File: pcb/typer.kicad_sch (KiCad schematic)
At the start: 48 parts, among them J2 3.5mm, SW0:10 SW0:3, SW0:11 SW0:2, SW0:12 SW0:1, SW0:7 SW0:6, SW0:8 SW0:5, SW0:9 SW0:4, SW1:10 SW1:3, SW1:11 SW1:2, SW1:12 SW1:1, SW1:13 SW1:0, SW1:9 SW1:4, SW2:10 SW2:3, SW2:11 SW2:2, SW2:12 SW2:1, SW2:13 SW2:0, SW2:7 SW2:6, SW2:8 SW2:5, SW2:9 SW2:4, SW3:10 SW3:3, SW3:11 SW3:2, SW3:12 SW3:1, SW3:13 SW3:0, SW3:8 SW3:5, SW3:9 SW3:4, SW4:10 SW4:3, SW4:11 SW4:2, SW4:12 SW4:1, SW4:13 SW4:0, SW4:7 SW4:6, SW4:8 SW4:5, SW4:9 SW4:4, SW5:10 SW5:3, SW5:11 SW5:2, SW5:12 SW5:1, SW5:13 SW5:0, SW5:7 SW5:6, SW5:8 SW5:5, SW5:9 SW5:4

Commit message: new project updates
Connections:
- net ROW0 is gone; now on an unnamed net: SW0:10.1, SW0:11.1, SW0:12.1, SW0:7.1, SW0:8.1, SW0:9.1, SX0:10.1, SX0:11.1
- net ROW1 is gone; now on an unnamed net: SW1:10.1, SW1:11.1, SW1:12.1, SW1:13.1, SW1:9.1, SX1:7.1, SX1:8.1
- net at D1:8.1 (A), SX1:8.2: now also D1:7.1 (A), D1:7.2 (K), D1:8.2 (K), SW0:10.4 (K), SW0:11.4 (K), SW0:7.4 (K), SW0:8.4 (K), SW1:10.4 (K), SW1:11.4 (K), SW2:10.4 (K), SW2:11.4 (K), SW2:7.4 (K), SW2:8.4 (K), SW3:10.4 (K), SW3:11.4 (K), SW3:8.4 (K), SX1:7.2
- net COL0: no longer names the net of SW1:13.4 (K), SW2:13.4 (K), SW3:13.4 (K)
- net COL0: no longer SW4:13.4 (K), SW5:13.4 (K)
- net COL1: no longer names the net of SW0:12.4 (K), SW1:12.4 (K), SW2:12.4 (K), SW3:12.4 (K)
- net COL1: no longer SW4:12.4 (K), SW5:12.4 (K)
- removed net COL10: SW0:10.4 (K), SW1:10.4 (K), SW2:10.4 (K), SW3:10.4 (K), SW4:10.4 (K), SW5:10.4 (K)
- removed net COL11: SW0:11.4 (K), SW1:11.4 (K), SW2:11.4 (K), SW3:11.4 (K), SW4:11.4 (K), SW5:11.4 (K)
- net COL4: no longer names the net of SW0:9.4 (K), SW1:9.4 (K), SW2:9.4 (K), SW3:9.4 (K)
- net COL4: no longer SW4:9.4 (K), SW5:9.4 (K)
- removed net COL5: D1:8.2 (K), SW0:8.4 (K), SW2:8.4 (K), SW3:8.4 (K), SW4:8.4 (K), SW5:8.4 (K)
- removed net COL6: D1:7.2 (K), SW0:7.4 (K), SW2:7.4 (K), SW4:7.4 (K), SW5:7.4 (K)
- net ROW2: no longer names the net of SW2:10.1, SW2:11.1, SW2:12.1, SW2:13.1, SW2:7.1, SW2:8.1, SW2:9.1
- removed net ROW3: SW3:10.1, SW3:11.1, SW3:12.1, SW3:13.1, SW3:8.1, SW3:9.1
- removed net ROW4: SW4:10.1, SW4:11.1, SW4:12.1, SW4:13.1, SW4:7.1, SW4:8.1, SW4:9.1
- removed net ROW5: SW5:10.1, SW5:11.1, SW5:12.1, SW5:13.1, SW5:7.1, SW5:8.1, SW5:9.1
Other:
- note added: "Mounting Holes"
- moved on the sheet: D1:7, D1:8, H99, J2, S1, S2, SW0:10, SW0:11, SW0:12, SW0:7, SW0:8, SW0:9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

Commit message: placement update
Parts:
- removed D1:7, D1:8: D, symbol Library:DIODE
- H99: footprint (none) -> Library:ErgoDOXmech
- J2: footprint (none) -> Library:4pin35mmAudio
- S1, S2: footprint (none) -> Library:STAB_PCB940
- SW0:0: renamed from SW5:13; value SW5:0 -> SW0:0; footprint (none) -> Library:MX_FLIP_XX
- SW0:1: renamed from SW4:13; value SW4:0 -> SW0:1; footprint (none) -> Library:MX_FLIP_XX
- SW0:2: renamed from SW3:13; value SW3:0 -> SW0:2; footprint (none) -> Library:MX_FLIP_XX
- SW0:3: renamed from SW2:13; value SW2:0 -> SW0:3; footprint (none) -> Library:MX_FLIP_XX
- SW0:4: renamed from SW1:13; value SW1:0 -> SW0:4; footprint (none) -> Library:MX_FLIP_DIODE
- SW1:0: renamed from SW5:12; value SW5:1 -> SW1:0; footprint (none) -> Library:MX_FLIP_DIODE
- SW1:1: renamed from SW4:12; value SW4:1 -> SW1:1; footprint (none) -> Library:MX_FLIP_DIODE
- SW1:2: renamed from SW3:12; value SW3:1 -> SW1:2; footprint (none) -> Library:MX_FLIP_DIODE
- SW1:3: renamed from SW2:12; value SW2:1 -> SW1:3; footprint (none) -> Library:MX_FLIP_DIODE
- SW1:4: renamed from SW1:12; value SW1:1 -> SW1:4; footprint (none) -> Library:MX_FLIP_DIODE
- SW2:0: renamed from SW5:11; value SW5:2 -> SW2:0; footprint (none) -> Library:MX_FLIP_DIODE
- SW2:1: renamed from SW4:11; value SW4:2 -> SW2:1; footprint (none) -> Library:MX_FLIP_DIODE
- SW2:2: renamed from SW3:11; value SW3:2 -> SW2:2; footprint (none) -> Library:MX_FLIP_DIODE
- SW2:3: renamed from SW2:11; value SW2:2 -> SW2:3; footprint (none) -> Library:MX_FLIP_DIODE
- SW2:4: renamed from SW1:11; value SW1:2 -> SW2:4; footprint (none) -> Library:MX_FLIP_DIODE
- SW3:0: renamed from SW5:10; value SW5:3 -> SW3:0; footprint (none) -> Library:MX_FLIP_DIODE
- SW3:1: renamed from SW4:10; value SW4:3 -> SW3:1; footprint (none) -> Library:MX_FLIP_DIODE
- SW3:2: renamed from SW3:10; value SW3:3 -> SW3:2; footprint (none) -> Library:MX_FLIP_DIODE
- SW3:3: renamed from SW2:10; value SW2:3 -> SW3:3; footprint (none) -> Library:MX_FLIP_DIODE
- SW3:4: renamed from SW1:10; value SW1:3 -> SW3:4; footprint (none) -> Library:MX_FLIP_DIODE
- SW4:0: renamed from SW5:9; value SW5:4 -> SW4:0; footprint (none) -> Library:MX_FLIP_DIODE
- SW4:1: renamed from SW4:9; value SW4:4 -> SW4:1; footprint (none) -> Library:MX_FLIP_DIODE
- SW4:2: renamed from SW3:9; value SW3:4 -> SW4:2; footprint (none) -> Library:MX_FLIP_DIODE
- SW4:3: renamed from SW2:9; value SW2:4 -> SW4:3; footprint (none) -> Library:MX_FLIP_DIODE
- SW4:4: renamed from SW1:9; value SW1:4 -> SW4:4; footprint (none) -> Library:MX_FLIP_DIODE
- SW5:0: renamed from SW5:8; value SW5:5 -> SW5:0; footprint (none) -> Library:MX_FLIP_DIODE
- SW5:1: renamed from SW4:8; value SW4:5 -> SW5:1; footprint (none) -> Library:MX_FLIP_DIODE
- SW5:2: renamed from SW3:8; value SW3:5 -> SW5:2; footprint (none) -> Library:MX_FLIP_DIODE
- SW5:3: renamed from SW2:8; value SW2:5 -> SW5:3; footprint (none) -> Library:MX_FLIP_DIODE
- SW5:4: renamed from SW0:11; value SW0:2 -> SW5:4; footprint (none) -> Library:MX_FLIP_DIODE
- SW6:0: renamed from SW5:7; value SW5:6 -> SW6:0; footprint (none) -> Library:MX_FLIP_DIODE
- SW6:1: renamed from SW4:7; value SW4:6 -> SW6:1; footprint (none) -> Library:MX_FLIP_DIODE
- SW6:2: renamed from SW2:7; value SW2:6 -> SW6:2; footprint (none) -> Library:MX_FLIP_DIODE
- SW6:3: renamed from SW0:12; value SW0:1 -> SW6:3; footprint (none) -> Library:MX_FLIP_DIODE
- SW6:4: renamed from SW0:10; value SW0:3 -> SW6:4; footprint (none) -> Library:MX_FLIP_DIODE
- SW7:2: renamed from SW0:7; value SW0:6 -> SW7:2; footprint (none) -> Library:MX_FLIP_DIODE
- SW7:3: renamed from SW0:8; value SW0:5 -> SW7:3; footprint (none) -> Library:MX_FLIP_DIODE
- SW7:4: renamed from SW0:9; value SW0:4 -> SW7:4; footprint (none) -> Library:MX_FLIP_DIODE
- SX5:4: renamed from SX1:7; value SX1:6 -> SX5:4; footprint (none) -> Library:MX_FLIP
- SX6:4: renamed from SX1:8; value SX1:5 -> SX6:4; footprint (none) -> Library:MX_FLIP
- SY5:4: renamed from SX0:11; value SX0:2 -> SY5:4; footprint (none) -> Library:MX_FLIP
- SY6:4: renamed from SX0:10; value SX0:3 -> SY6:4; footprint (none) -> Library:MX_FLIP
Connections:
- net at SW6:4.2, SW6:4.3 (A), SY6:4.2: now also SX6:4.2
- net COLUMN6: now reaches SW6:1.1
- net COLUMN6: now also SW6:0.1, SW6:2.1, SW6:3.1, SW6:4.1, SX6:4.1, SY6:4.1
- net ROW1: now reaches SW6:1.4 (K)
- net ROW1: now also SW0:1.4 (K), SW1:1.4 (K), SW2:1.4 (K), SW3:1.4 (K), SW4:1.4 (K), SW5:1.4 (K)
- net COLUMN5: now reaches SW5:1.1
- net COLUMN5: now also SW5:0.1, SW5:2.1, SW5:3.1, SW5:4.1, SX5:4.1, SY5:4.1
- net COLUMN1: now reaches SW1:1.1
- net COLUMN1: now also SW1:0.1, SW1:2.1, SW1:3.1, SW1:4.1
- net COLUMN2: now reaches SW2:1.1
- net COLUMN2: now also SW2:0.1, SW2:2.1, SW2:3.1, SW2:4.1
- net COLUMN3: now reaches SW3:1.1
- net COLUMN3: now also SW3:0.1, SW3:2.1, SW3:3.1, SW3:4.1
- net COLUMN4: now reaches SW4:1.1
- net COLUMN4: now also SW4:0.1, SW4:2.1, SW4:3.1, SW4:4.1
- net COLUMN0: now reaches SW0:1.1
- net COLUMN0: now also SW0:0.1, SW0:2.1, SW0:3.1, SW0:4.1
- net ROW4: now reaches SW4:4.4 (K), SW7:4.4 (K)
- net ROW4: now also SW0:4.4 (K), SW1:4.4 (K), SW2:4.4 (K), SW3:4.4 (K), SW5:4.4 (K), SW6:4.4 (K); no longer SW4:2.4 (K), SW4:3.4 (K)
- net at SW5:4.2, SW5:4.3 (A), SY5:4.2: now also SX5:4.2
- net ROW0: now reaches SW0:0.4 (K)
- net ROW0: now also SW1:0.4 (K), SW2:0.4 (K), SW3:0.4 (K), SW4:0.4 (K), SW5:0.4 (K), SW6:0.4 (K)
- new net COLUMN7: SW7:2.1, SW7:3.1, SW7:4.1
- new net ROW2: SW0:2.4 (K), SW1:2.4 (K), SW2:2.4 (K), SW3:2.4 (K), SW4:2.4 (K), SW5:2.4 (K), SW6:2.4 (K), SW7:2.4 (K)
- new net ROW3: SW7:3.4 (K)
- now unconnected: SW0:3.4 (K), SW1:3.4 (K), SW2:3.4 (K), SW3:3.4 (K), SW5:3.4 (K), SW6:3.4 (K)
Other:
- moved on the sheet: SW5:4, SW6:2, SW6:3, SW6:4, SW7:2, SW7:3, SW7:4, SX5:4, SX6:4, SY5:4, SY6:4

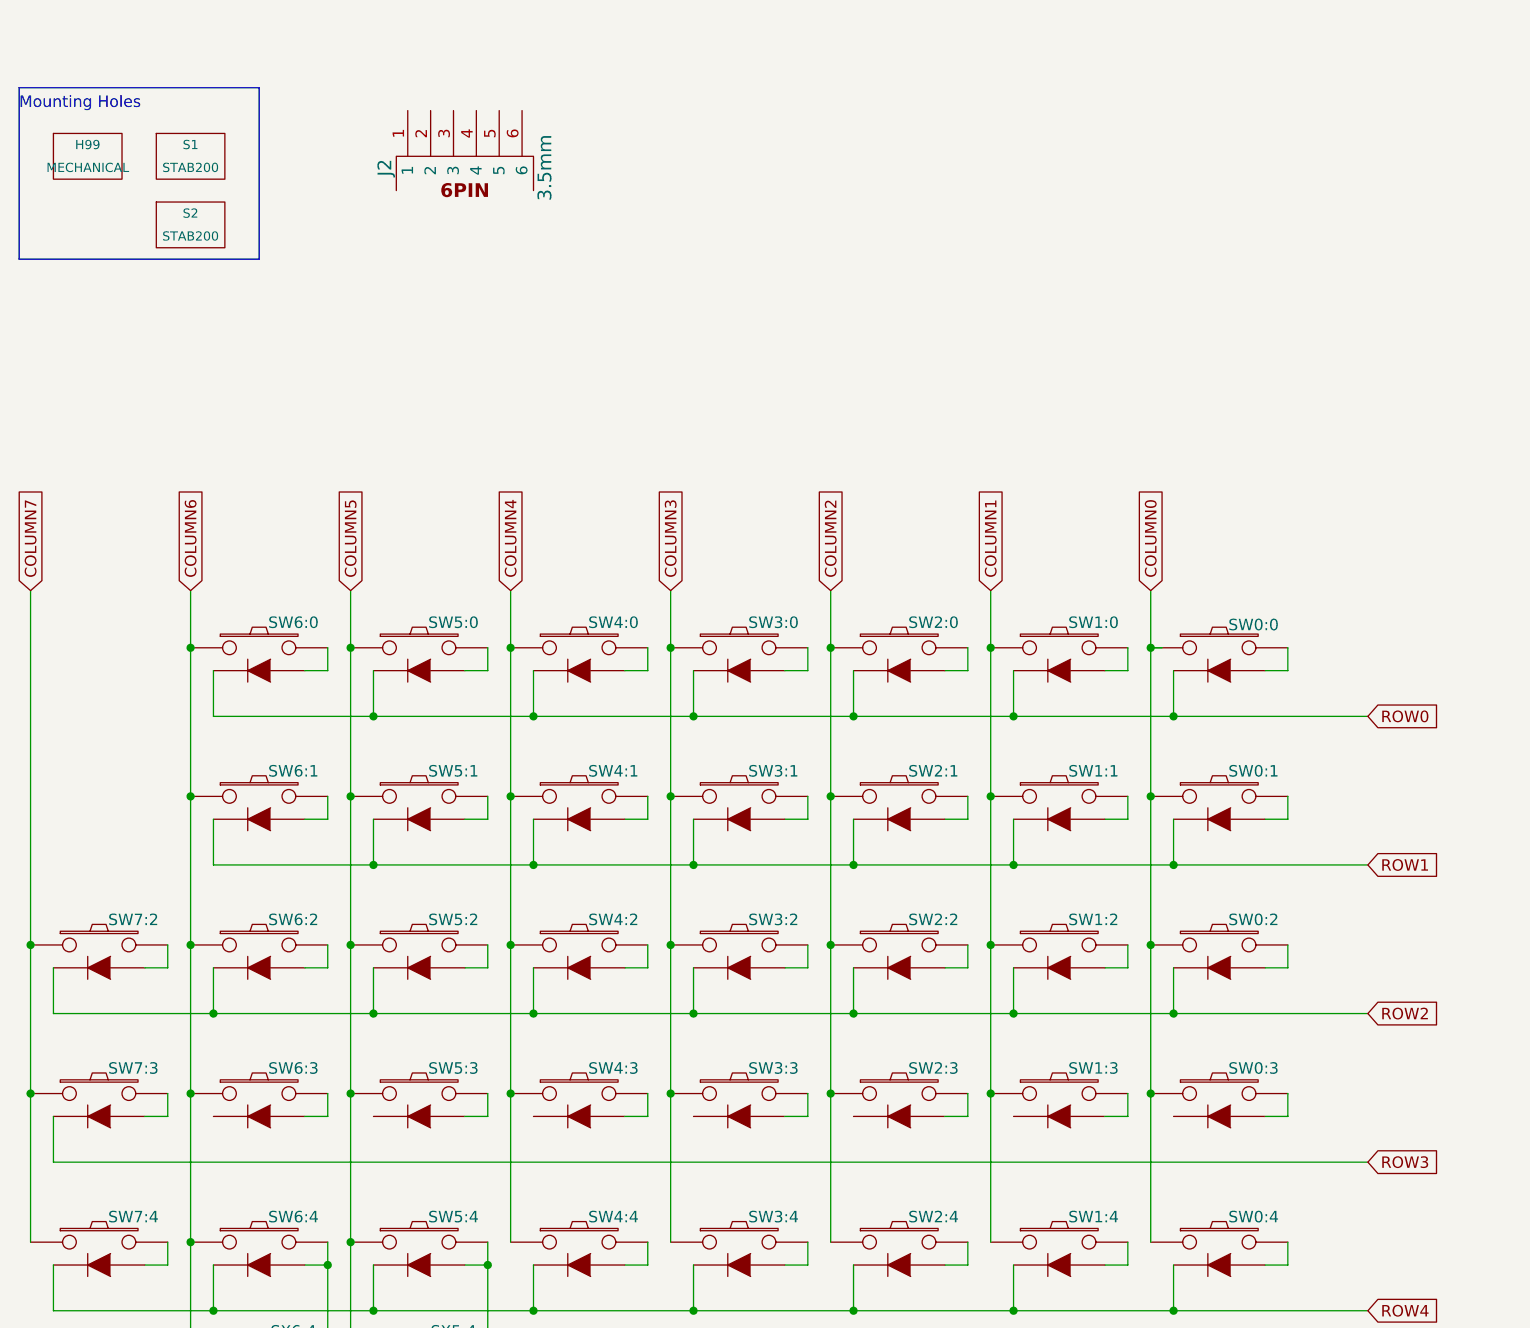
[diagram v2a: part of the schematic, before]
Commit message: row track layout added
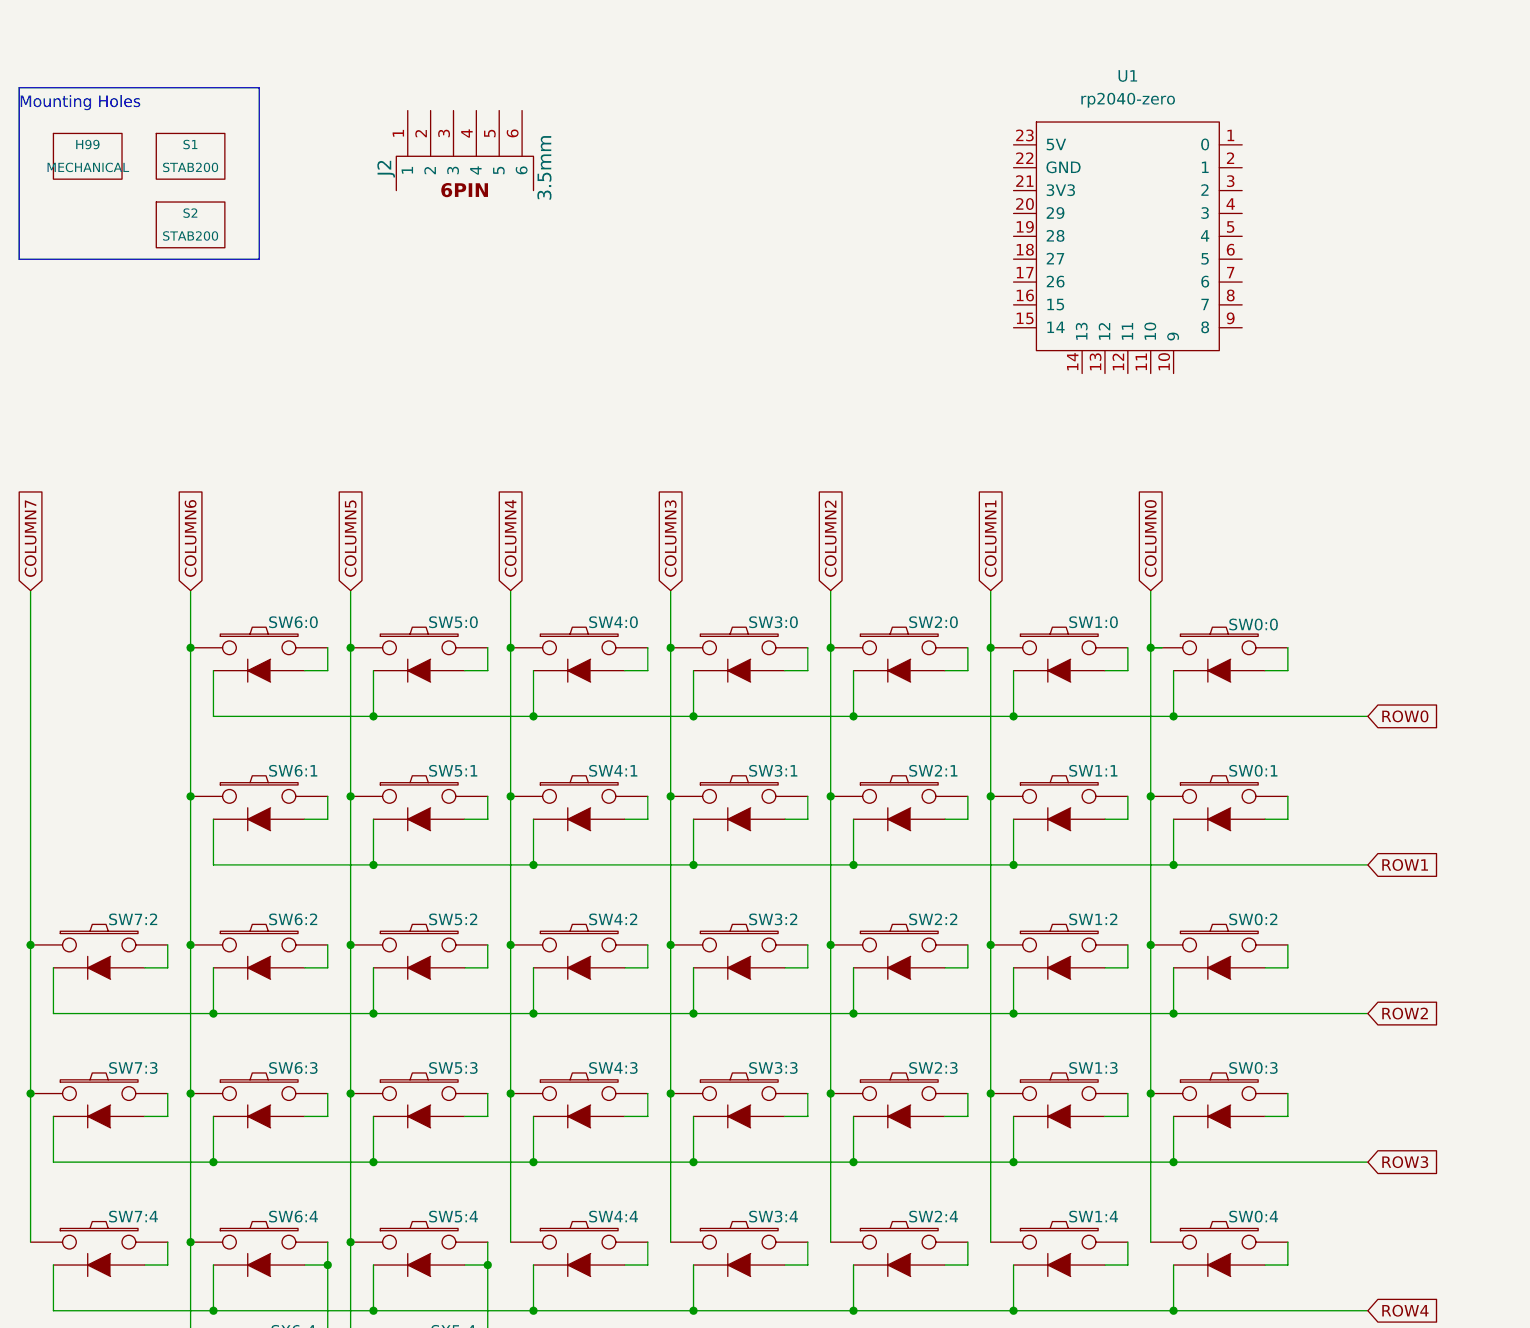
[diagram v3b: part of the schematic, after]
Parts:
- added U1: rp2040-zero, mcu:rp2040-zero-tht, symbol mcu:rp2040-zero
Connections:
- net ROW3: now also SW0:3.4 (K), SW1:3.4 (K), SW2:3.4 (K), SW3:3.4 (K), SW4:3.4 (K), SW5:3.4 (K), SW6:3.4 (K)
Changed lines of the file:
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@@
     (date "29 sep 2012")
   )
+  (junction (at 59.69 143.51) (diameter 0) (color 0 0 0 0)
+  )
   (junction (at 110.49 102.87) (diameter 0) (color 0 0 0 0)
   )
@@
   (junction (at 148.59 127) (diameter 0) (color 0 0 0 0)
   )
+  (junction (at 130.81 143.51) (diameter 0) (color 0 0 0 0)
+  )
+  (junction (at 41.91 143.51) (diameter 0) (color 0 0 0 0)
+  )
   (junction (at 74.93 135.89) (diameter 0) (color 0 0 0 0)
   )
@@
   (junction (at 130.81 93.98) (diameter 0) (color 0 0 0 0)
   )
+  (junction (at 77.47 143.51) (diameter 0) (color 0 0 0 0)
+  )
   (junction (at 146.05 102.87) (diameter 0) (color 0 0 0 0)
   )
@@
   (junction (at 95.25 110.49) (diameter 0) (color 0 0 0 0)
   )
+  (junction (at 113.03 143.51) (diameter 0) (color 0 0 0 0)
+  )
   (junction (at 92.71 86.36) (diameter 0) (color 0 0 0 0)
   )
@@
   (junction (at 57.15 165.1) (diameter 0) (color 0 0 0 0)
   )
+  (junction (at 148.59 143.51) (diameter 0) (color 0 0 0 0)
+  )
   (junction (at 39.37 135.89) (diameter 0) (color 0 0 0 0)
   )
+  (junction (at 95.25 143.51) (diameter 0) (color 0 0 0 0)
+  )
   (junction (at 148.59 160.02) (diameter 0) (color 0 0 0 0)
   )
@@
     (stroke (width 0) (type default))
   )
+  (wire (pts (xy 148.59 138.43) (xy 148.59 143.51))
+    (stroke (width 0) (type default))
+  )
   (wire (pts (xy 52.07 138.43) (xy 54.61 138.43))
     (stroke (width 0) (type default))
@@
     (stroke (width 0) (type default))
   )
+  (wire (pts (xy 41.91 143.51) (xy 59.69 143.51))
+    (stroke (width 0) (type default))
+  )
   (wire (pts (xy 146.05 86.36) (xy 146.05 80.01))
     (stroke (width 0) (type default))
@@
     (stroke (width 0) (type default))
   )
+  (wire (pts (xy 95.25 138.43) (xy 95.25 143.51))
+    (stroke (width 0) (type default))
+  )
   (wire (pts (xy 95.25 160.02) (xy 113.03 160.02))
     (stroke (width 0) (type default))
@@
     (stroke (width 0) (type default))
   )
+  (wire (pts (xy 130.81 138.43) (xy 130.81 143.51))
+    (stroke (width 0) (type default))
+  )
   (wire (pts (xy 158.75 138.43) (xy 161.29 138.43))
     (stroke (width 0) (type default))
@@
     (stroke (width 0) (type default))
   )
+  (wire (pts (xy 113.03 143.51) (xy 130.81 143.51))
+    (stroke (width 0) (type default))
+  )
   (wire (pts (xy 130.81 160.02) (xy 148.59 160.02))
     (stroke (width 0) (type default))
@@
     (stroke (width 0) (type default))
   )
-  (wire (pts (xy 24.13 143.51) (xy 170.18 143.51))
+  (wire (pts (xy 24.13 143.51) (xy 41.91 143.51))
     (stroke (width 0) (type default))
   )
@@
     (stroke (width 0) (type default))
   )
+  (wire (pts (xy 41.91 138.43) (xy 41.91 143.51))
+    (stroke (width 0) (type default))
+  )
   (wire (pts (xy 113.03 121.92) (xy 113.03 127))
     (stroke (width 0) (type default))
@@
     (stroke (width 0) (type default))
   )
+  (wire (pts (xy 77.47 143.51) (xy 95.25 143.51))
+    (stroke (width 0) (type default))
+  )
   (wire (pts (xy 146.05 135.89) (xy 146.05 152.4))
     (stroke (width 0) (type default))
@@
     (stroke (width 0) (type default))
   )
+  (wire (pts (xy 95.25 143.51) (xy 113.03 143.51))
+    (stroke (width 0) (type default))
+  )
   (wire (pts (xy 41.91 93.98) (xy 59.69 93.98))
     (stroke (width 0) (type default))
@@
     (stroke (width 0) (type default))
   )
+  (wire (pts (xy 113.03 138.43) (xy 113.03 143.51))
+    (stroke (width 0) (type default))
+  )
   (wire (pts (xy 95.25 105.41) (xy 95.25 110.49))
     (stroke (width 0) (type default))
@@
     (stroke (width 0) (type default))
   )
+  (wire (pts (xy 59.69 143.51) (xy 77.47 143.51))
+    (stroke (width 0) (type default))
+  )
   (wire (pts (xy 36.83 121.92) (xy 36.83 119.38))
     (stroke (width 0) (type default))
   )
+  (wire (pts (xy 59.69 138.43) (xy 59.69 143.51))
+    (stroke (width 0) (type default))
+  )
   (wire (pts (xy 148.59 160.02) (xy 170.18 160.02))
     (stroke (width 0) (type default))
@@
     (stroke (width 0) (type default))
   )
+  (wire (pts (xy 77.47 138.43) (xy 77.47 143.51))
+    (stroke (width 0) (type default))
+  )
   (wire (pts (xy 95.25 121.92) (xy 95.25 127))
     (stroke (width 0) (type default))
@@
     (stroke (width 0) (type default))
   )
+  (wire (pts (xy 148.59 143.51) (xy 170.18 143.51))
+    (stroke (width 0) (type default))
+  )
   (wire (pts (xy 59.69 105.41) (xy 59.69 110.49))
     (stroke (width 0) (type default))
@@
   )
   (wire (pts (xy 123.19 88.9) (xy 125.73 88.9))
+    (stroke (width 0) (type default))
+  )
+  (wire (pts (xy 130.81 143.51) (xy 148.59 143.51))
     (stroke (width 0) (type default))
   )
@@
         )
       )
+    )
+  )
+  (symbol (lib_id "mcu:rp2040-zero") (at 143.51 39.37 0) (unit 1)
+    (in_bom yes) (on_board yes) (dnp no) (fields_autoplaced)
+    (property "Reference" "U1" (at 143.51 22.86 0)
+      (effects (font (size 1.27 1.27)))
+    )
+    (property "Value" "rp2040-zero" (at 143.51 25.4 0)
+      (effects (font (size 1.27 1.27)))
+    )
+    (property "Footprint" "mcu:rp2040-zero-tht" (at 134.62 34.29 0)
+      (effects (font (size 1.27 1.27)) hide)
+    )
+    (property "Datasheet" "" (at 134.62 34.29 0)
+      (effects (font (size 1.27 1.27)) hide)
+    )
+    (pin "1")
+    (pin "10")
+    (pin "11")
+    (pin "12")
+    (pin "13")
+    (pin "14")
+    (pin "15")
+    (pin "16")
+    (pin "17")
+    (pin "18")
+    (pin "19")
+    (pin "2")
+    (pin "20")
+    (pin "21")
+    (pin "22")
+    (pin "23")
+    (pin "3")
+    (pin "4")
+    (pin "5")
+    (pin "6")
+    (pin "7")
+    (pin "8")
+    (pin "9")
+    (instances
+      (project "typer"
+        (path "/4d3b8a82-ffd9-4462-8856-ef55fc4ce56b"
+          (reference "U1") (unit 1)
+        )
+      )

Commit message: column traces
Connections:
- net COLUMN0: now also U1.3 (2)
- net COLUMN1: now also U1.4 (3)
- net COLUMN2: now also U1.5 (4)
- net COLUMN3: now also U1.6 (5)
- net COLUMN4: now also U1.7 (6)
- net COLUMN5: now also U1.8 (7)
- net COLUMN6: now also U1.9 (8)
- net COLUMN7: now also U1.10 (9)
- net GND: now also J2.2, U1.22 (GND)
- net ROW0: now also U1.15 (14)
- net ROW1: now also U1.16 (15)
- net ROW2: now also U1.17 (26)
- net ROW3: now also U1.18 (27)
- net ROW4: now also U1.19 (28)
- net 5V: now reaches J2.3
- net 5V: now also U1.23 (5V)
- net RX: now reaches J2.4
- net RX: now also U1.2 (1)
- net TX: now reaches J2.5
- net TX: now also U1.1 (0)
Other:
- moved on the sheet: J2, U1
